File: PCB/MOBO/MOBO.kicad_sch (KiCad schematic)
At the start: 19 parts

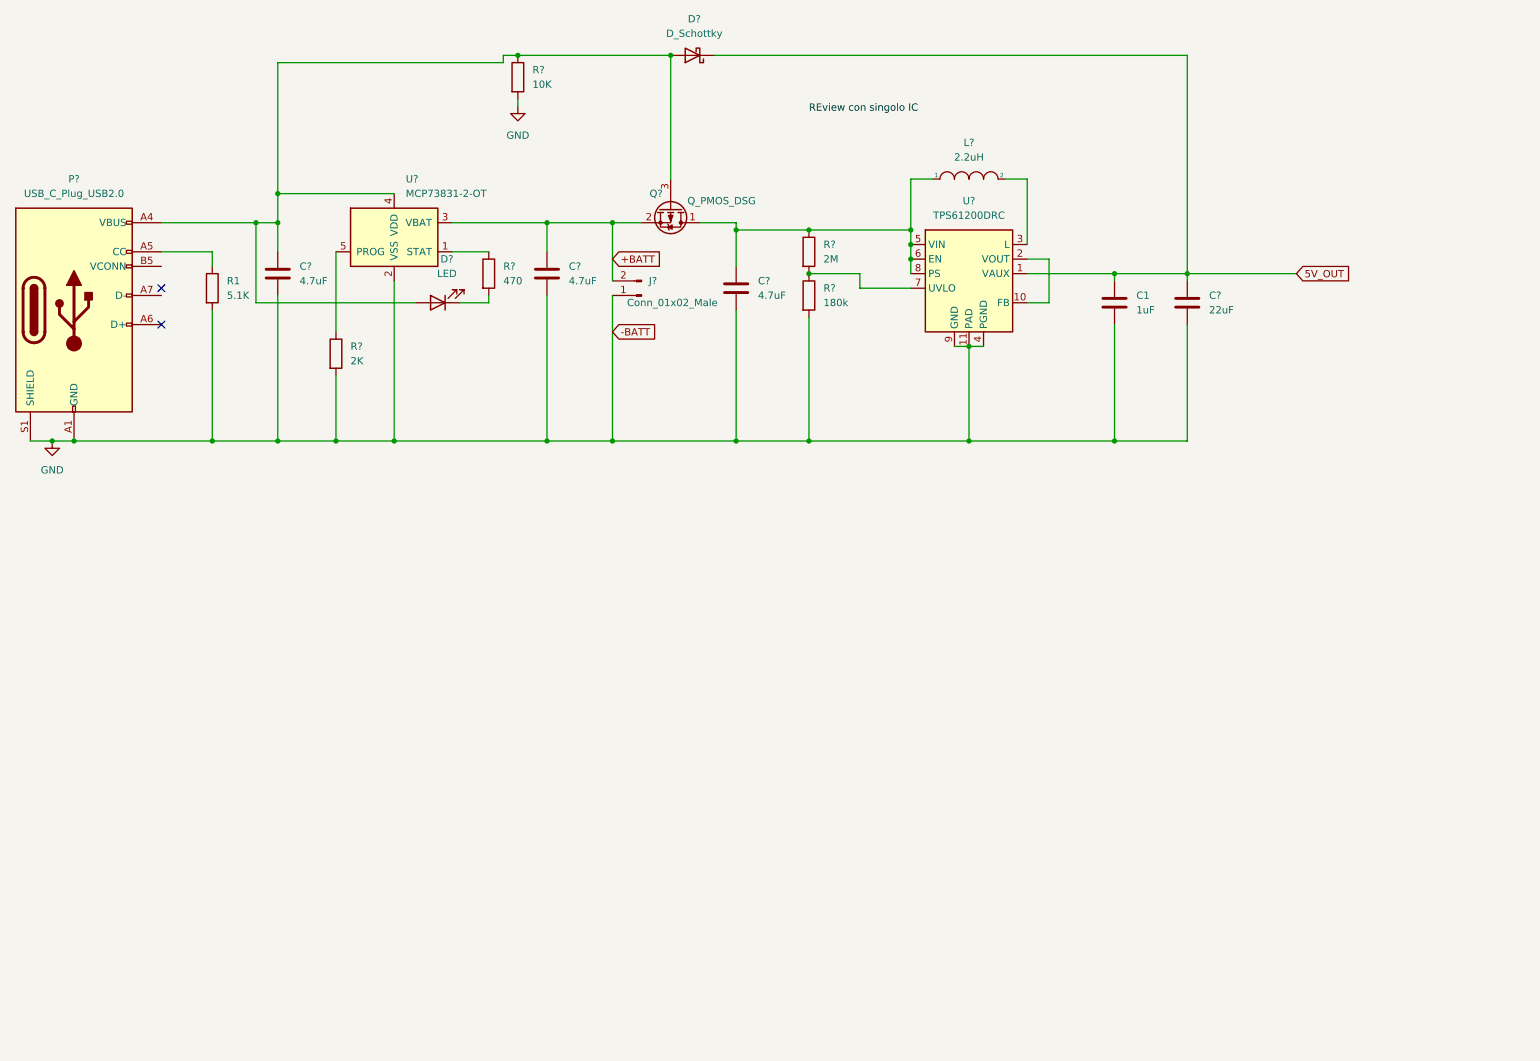
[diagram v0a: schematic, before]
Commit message: Added secondary power and charging solution
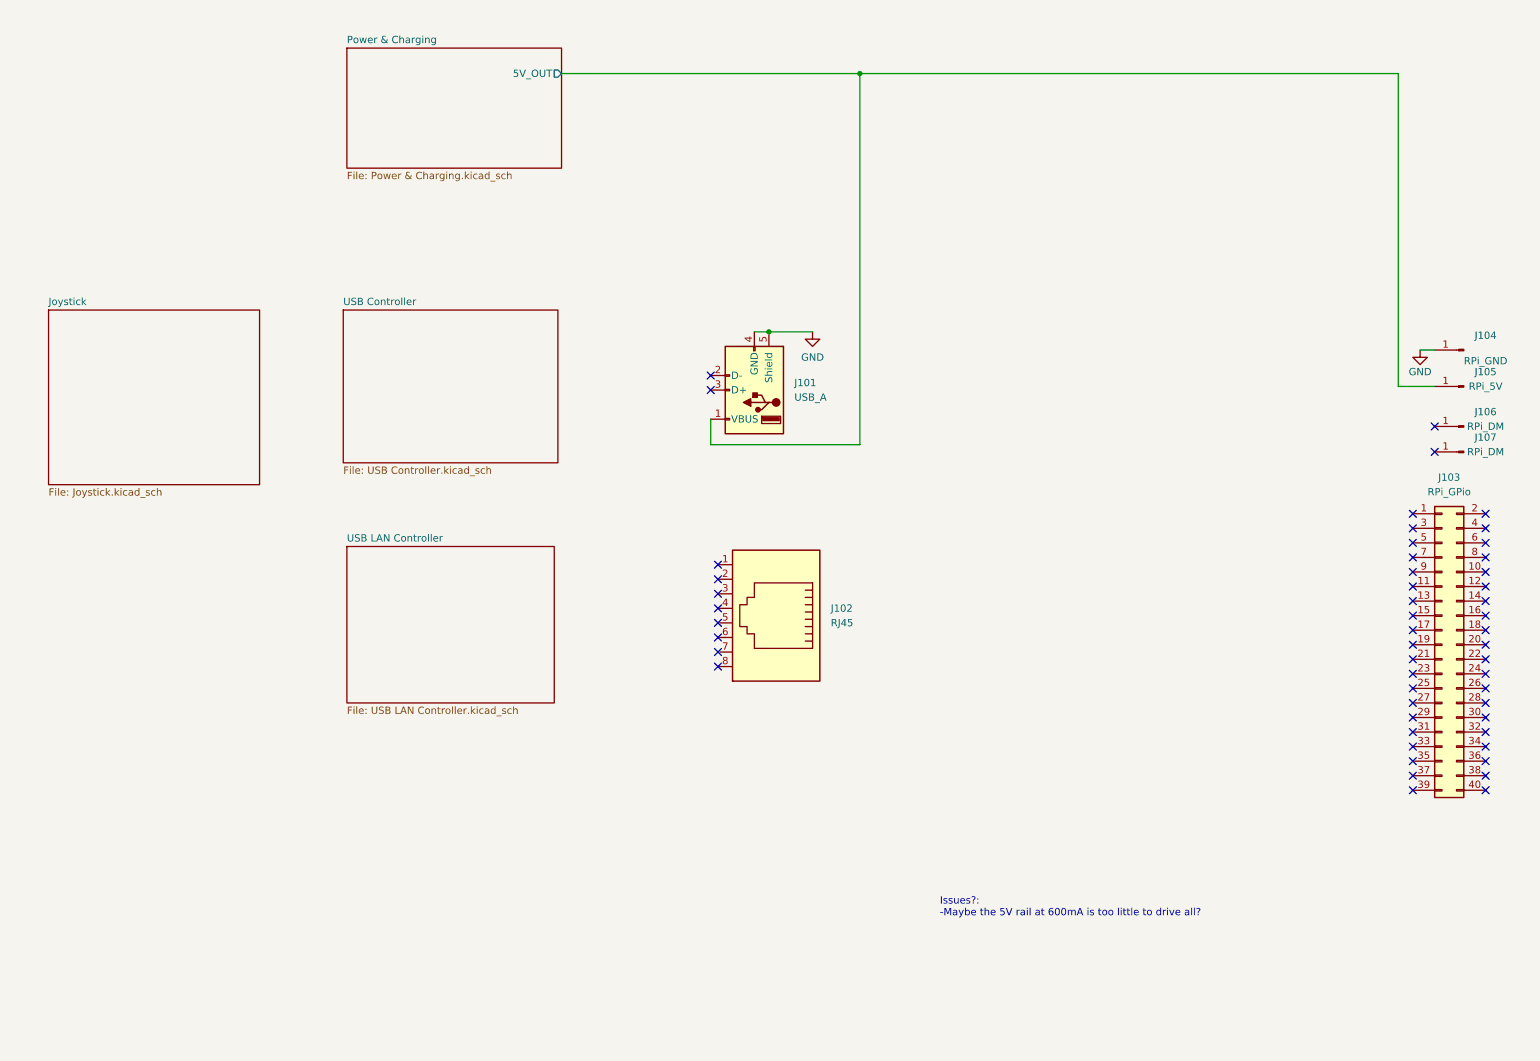
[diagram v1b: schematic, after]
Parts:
- removed C1: 1uF, symbol Device:C
- removed C? (x3): 4.7uF, symbol Device:C
- removed C?: 22uF, symbol Device:C
- removed D?: D_Schottky, symbol Device:D_Schottky
- removed D?: LED, symbol Device:LED
- removed J?: Conn_01x02_Male, symbol Connector:Conn_01x02_Male
- removed L?: 2.2uH, symbol pspice:INDUCTOR
- removed P?: USB_C_Plug_USB2.0, symbol Connector:USB_C_Plug_USB2.0
- removed Q?: Q_PMOS_DSG, symbol Device:Q_PMOS_DSG
- removed R1: 5.1K, symbol Device:R
- removed R?: 2M, symbol Device:R
- removed R?: 10K, symbol Device:R
- removed R?: 2K, symbol Device:R
- removed R?: 470, symbol Device:R
- removed R?: 180k, symbol Device:R
- removed U?: MCP73831-2-OT, Package_TO_SOT_SMD:SOT-23-5, symbol Battery_Management:MCP73831-2-OT
- removed U?: TPS61200DRC, Package_SON:Texas_S-PVSON-N10_ThermalVias, symbol Regulator_Switching:TPS61200DRC
- added J101: USB_A, symbol Connector:USB_A
- added J102: RJ45, symbol Connector:RJ45
- added J103: RPi_GPio, MountingHole:MountingHole_2.2mm_M2_DIN965_Pad, symbol Connector_Generic:Conn_02x20_Odd_Even
- added J104: RPi_GND, TestPoint:TestPoint_Pad_1.5x1.5mm, symbol Connector:Conn_01x01_Male
- added J105: RPi_5V, TestPoint:TestPoint_Pad_1.5x1.5mm, symbol Connector:Conn_01x01_Male
- added J106, J107: RPi_DM, TestPoint:TestPoint_Pad_1.5x1.5mm, symbol Connector:Conn_01x01_Male
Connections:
- net GND: now also J101.4 (GND), J101.5 (Shield), J104.1 (Pin_1)
- new net Power & Charging/5V_OUT: J101.1 (VBUS), J105.1 (Pin_1)
- no-connect marks 2 -> 52
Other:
- added sheet Joystick (Joystick.kicad_sch)
- added sheet Power & Charging (Power & Charging.kicad_sch)
- added sheet USB Controller (USB Controller.kicad_sch)
- added sheet USB LAN Controller (USB LAN Controller.kicad_sch)
- note added: "Issues?: -Maybe the 5V rail at 600mA is too little to drive all?"
- title: (none) -> Power Circuit

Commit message: added full atmega circuit and programming interface
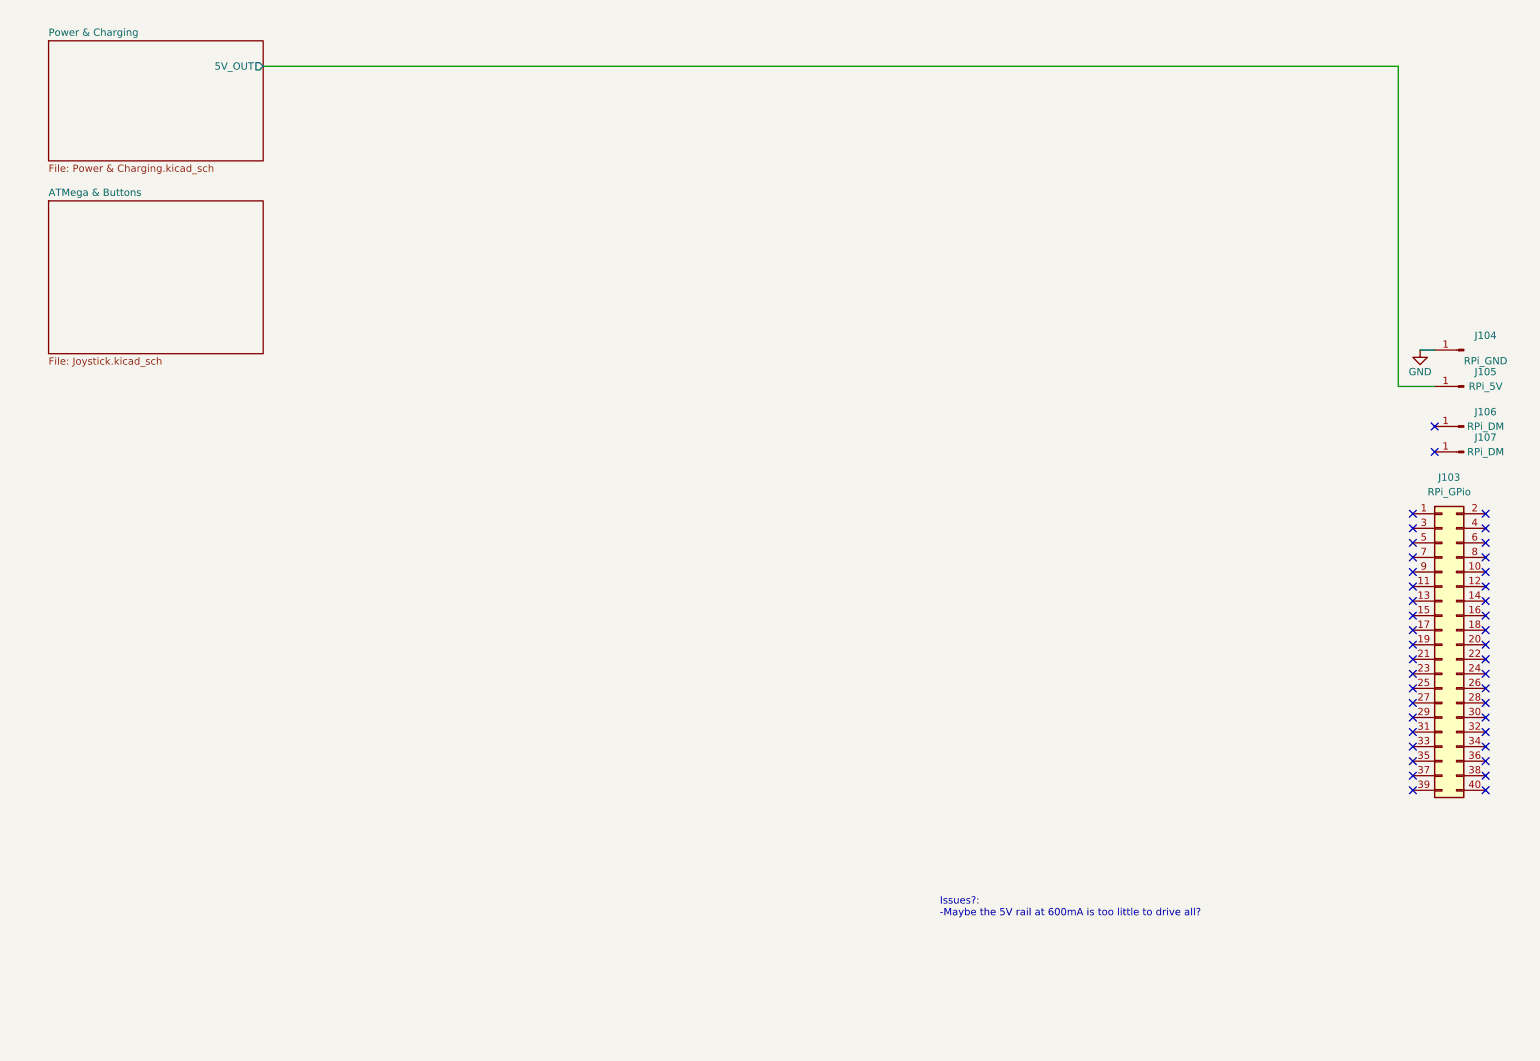
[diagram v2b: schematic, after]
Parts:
- removed J101: USB_A, symbol Connector:USB_A
- removed J102: RJ45, symbol Connector:RJ45
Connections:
- no-connect marks 52 -> 42
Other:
- sheet Joystick renamed ATMega & Buttons
- removed sheet USB Controller
- removed sheet USB LAN Controller
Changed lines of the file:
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@@
     (rev "0.1")
   )
-  (junction (at 147.955 68.58) (diameter 0) (color 0 0 0 0)
-  )
-  (junction (at 163.83 23.495) (diameter 0) (color 0 0 0 0)
-  )
   (no_connect (at 273.05 138.43))
-  (no_connect (at 139.065 116.84))
   (no_connect (at 260.35 128.27))
   (no_connect (at 273.05 128.27))
   (no_connect (at 273.05 123.19))
   (no_connect (at 273.05 130.81))
-  (no_connect (at 139.065 109.22))
   (no_connect (at 260.35 107.95))
-  (no_connect (at 139.065 121.92))
-  (no_connect (at 139.065 114.3))
-  (no_connect (at 139.065 111.76))
   (no_connect (at 260.35 135.89))
   (no_connect (at 264.16 89.535))
@@
   (no_connect (at 273.05 100.33))
   (no_connect (at 260.35 138.43))
-  (no_connect (at 139.065 127))
   (no_connect (at 260.35 130.81))
   (no_connect (at 260.35 118.11))
-  (no_connect (at 139.065 119.38))
   (no_connect (at 273.05 118.11))
   (no_connect (at 273.05 125.73))
-  (no_connect (at 137.795 78.74))
   (no_connect (at 273.05 143.51))
   (no_connect (at 260.35 110.49))
@@
   (no_connect (at 260.35 100.33))
   (no_connect (at 260.35 123.19))
-  (no_connect (at 137.795 76.2))
   (no_connect (at 273.05 146.05))
   (no_connect (at 260.35 133.35))
@@
   (no_connect (at 273.05 140.97))
   (no_connect (at 260.35 115.57))
-  (no_connect (at 139.065 124.46))
   (no_connect (at 260.35 105.41))
   (no_connect (at 273.05 107.95))
@@
   (no_connect (at 273.05 148.59))
   (no_connect (at 273.05 102.87))
-  (wire (pts (xy 257.81 23.495) (xy 257.81 78.105))
+  (wire (pts (xy 257.81 22.225) (xy 257.81 78.105))
     (stroke (width 0) (type default))
   )
@@
     (stroke (width 0) (type default))
   )
-  (wire (pts (xy 137.795 83.82) (xy 137.795 88.265))
-    (stroke (width 0) (type default))
-  )
-  (wire (pts (xy 145.415 68.58) (xy 147.955 68.58))
-    (stroke (width 0) (type default))
-  )
-  (wire (pts (xy 163.83 88.265) (xy 163.83 23.495))
-    (stroke (width 0) (type default))
-  )
-  (wire (pts (xy 111.76 23.495) (xy 163.83 23.495))
-    (stroke (width 0) (type default))
-  )
-  (wire (pts (xy 163.83 23.495) (xy 257.81 23.495))
+  (wire (pts (xy 59.69 22.225) (xy 257.81 22.225))
     (stroke (width 0) (type default))
   )
   (wire (pts (xy 257.81 78.105) (xy 264.16 78.105))
-    (stroke (width 0) (type default))
-  )
-  (wire (pts (xy 137.795 88.265) (xy 163.83 88.265))
-    (stroke (width 0) (type default))
-  )
-  (wire (pts (xy 147.955 68.58) (xy 155.575 68.58))
     (stroke (width 0) (type default))
   )
@@
     )
   )
-  (symbol (lib_id "power:GND") (at 155.575 68.58 0) (unit 1)
-    (in_bom yes) (on_board yes) (dnp no) (fields_autoplaced)
-    (property "Reference" "#PWR0101" (at 155.575 74.93 0)
-      (effects (font (size 1.27 1.27)) hide)
-    )
-    (property "Value" "GND" (at 155.575 73.025 0)
-      (effects (font (size 1.27 1.27)))
-    )
-    (property "Footprint" "" (at 155.575 68.58 0)
-      (effects (font (size 1.27 1.27)) hide)
-    )
-    (property "Datasheet" "" (at 155.575 68.58 0)
-      (effects (font (size 1.27 1.27)) hide)
-    )
-    (pin "1")
-    (instances
-      (project "MOBO"
-        (path "/2d62a3c1-c4f2-4921-9f6b-8dc8aef69d64"
-          (reference "#PWR0101") (unit 1)
-        )
-      )
-    )
-  )
-  (symbol (lib_id "Connector:USB_A") (at 145.415 78.74 180) (unit 1)
-    (in_bom yes) (on_board yes) (dnp no) (fields_autoplaced)
-    (property "Reference" "J101" (at 152.4 77.4699 0)
-      (effects (font (size 1.27 1.27)) (justify right))
-    )
-    (property "Value" "USB_A" (at 152.4 80.0099 0)
-      (effects (font (size 1.27 1.27)) (justify right))
-    )
-    (property "Footprint" "" (at 141.605 77.47 0)
-      (effects (font (size 1.27 1.27)) hide)
-    )
-    (property "Datasheet" " ~" (at 141.605 77.47 0)
-      (effects (font (size 1.27 1.27)) hide)
-    )
-    (pin "1")
-    (pin "2")
-    (pin "3")
-    (pin "4")
-    (pin "5")
-    (instances
-      (project "MOBO"
-        (path "/2d62a3c1-c4f2-4921-9f6b-8dc8aef69d64"
-          (reference "J101") (unit 1)
-        )
-      )
-    )
-  )
   (symbol (lib_id "Connector:Conn_01x01_Male") (at 269.24 85.09 180) (unit 1)
     (in_bom yes) (on_board yes) (dnp no)
@@
     )
   )
-  (symbol (lib_id "Connector:RJ45") (at 149.225 116.84 180) (unit 1)
-    (in_bom yes) (on_board yes) (dnp no) (fields_autoplaced)
-    (property "Reference" "J102" (at 158.75 116.8399 0)
-      (effects (font (size 1.27 1.27)) (justify right))
-    )
-    (property "Value" "RJ45" (at 158.75 119.3799 0)
-      (effects (font (size 1.27 1.27)) (justify right))
-    )
-    (property "Footprint" "" (at 149.225 117.475 90)
-      (effects (font (size 1.27 1.27)) hide)
-    )
-    (property "Datasheet" "~" (at 149.225 117.475 90)
-      (effects (font (size 1.27 1.27)) hide)
-    )
-    (pin "1")
-    (pin "2")
-    (pin "3")
-    (pin "4")
-    (pin "5")
-    (pin "6")
-    (pin "7")
-    (pin "8")
-    (instances
-      (project "MOBO"
-        (path "/2d62a3c1-c4f2-4921-9f6b-8dc8aef69d64"
-          (reference "J102") (unit 1)
-        )
-      )
-    )
-  )
-  (sheet (at 73.66 64.77) (size 37.465 26.67) (fields_autoplaced)
+  (sheet (at 22.225 45.72) (size 37.465 26.67) (fields_autoplaced)
     (stroke (width 0.1524) (type solid))
     (fill (color 0 0 0 0.0000))
-    (property "Sheetname" "USB Controller" (at 73.66 64.0584 0)
+    (property "Sheetname" "ATMega & Buttons" (at 22.225 45.0084 0)
       (effects (font (size 1.27 1.27)) (justify left bottom))
     )
-    (property "Sheetfile" "USB Controller.kicad_sch" (at 73.66 92.0246 0)
+    (property "Sheetfile" "Joystick.kicad_sch" (at 22.225 72.9746 0)
       (effects (font (size 1.27 1.27)) (justify left top))
     )
     (instances
       (project "MOBO"
-        (path "/2d62a3c1-c4f2-4921-9f6b-8dc8aef69d64" (page "3"))
-      )
-    )
-  )
-  (sheet (at 22.225 64.77) (size 36.83 30.48) (fields_autoplaced)
+        (path "/2d62a3c1-c4f2-4921-9f6b-8dc8aef69d64" (page "5"))
+      )
+    )
+  )
+  (sheet (at 22.225 17.78) (size 37.465 20.955) (fields_autoplaced)
     (stroke (width 0.1524) (type solid))
     (fill (color 0 0 0 0.0000))
-    (property "Sheetname" "Joystick" (at 22.225 64.0584 0)
+    (property "Sheetname" "Power & Charging" (at 22.225 17.0684 0)
       (effects (font (size 1.27 1.27)) (justify left bottom))
     )
-    (property "Sheetfile" "Joystick.kicad_sch" (at 22.225 95.8346 0)
+    (property "Sheetfile" "Power & Charging.kicad_sch" (at 22.225 39.3196 0)
       (effects (font (size 1.27 1.27)) (justify left top))
     )
-    (instances
-      (project "MOBO"
-        (path "/2d62a3c1-c4f2-4921-9f6b-8dc8aef69d64" (page "5"))
-      )
-    )
-  )
-  (sheet (at 74.295 19.05) (size 37.465 20.955) (fields_autoplaced)
-    (stroke (width 0.1524) (type solid))
-    (fill (color 0 0 0 0.0000))
-    (property "Sheetname" "Power & Charging" (at 74.295 18.3384 0)
-      (effects (font (size 1.27 1.27)) (justify left bottom))
-    )
-    (property "Sheetfile" "Power & Charging.kicad_sch" (at 74.295 40.5896 0)
-      (effects (font (size 1.27 1.27)) (justify left top))
-    )
-    (pin "5V_OUT" output (at 111.76 23.495 0)
+    (pin "5V_OUT" output (at 59.69 22.225 0)
       (effects (font (size 1.27 1.27)) (justify right))
     )
@@
       )
     )
-  )
-  (sheet (at 74.295 106.045) (size 36.195 27.305) (fields_autoplaced)
-    (stroke (width 0.1524) (type solid))
-    (fill (color 0 0 0 0.0000))
-    (property "Sheetname" "USB LAN Controller" (at 74.295 105.3334 0)
-      (effects (font (size 1.27 1.27)) (justify left bottom))
-    )
-    (property "Sheetfile" "USB LAN Controller.kicad_sch" (at 74.295 133.9346 0)
-      (effects (font (size 1.27 1.27)) (justify left top))
-    )
-    (instances
-      (project "MOBO"
-        (path "/2d62a3c1-c4f2-4921-9f6b-8dc8aef69d64" (page "4"))
-      )
-    )
